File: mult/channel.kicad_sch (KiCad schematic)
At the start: 17 parts, among them J1 Eurorack_Mono_Jack, J2 Eurorack_Mono_Jack, J3 Eurorack_Mono_Jack_No_S, J4 Eurorack_Mono_Jack_No_S, U1 OPA1679

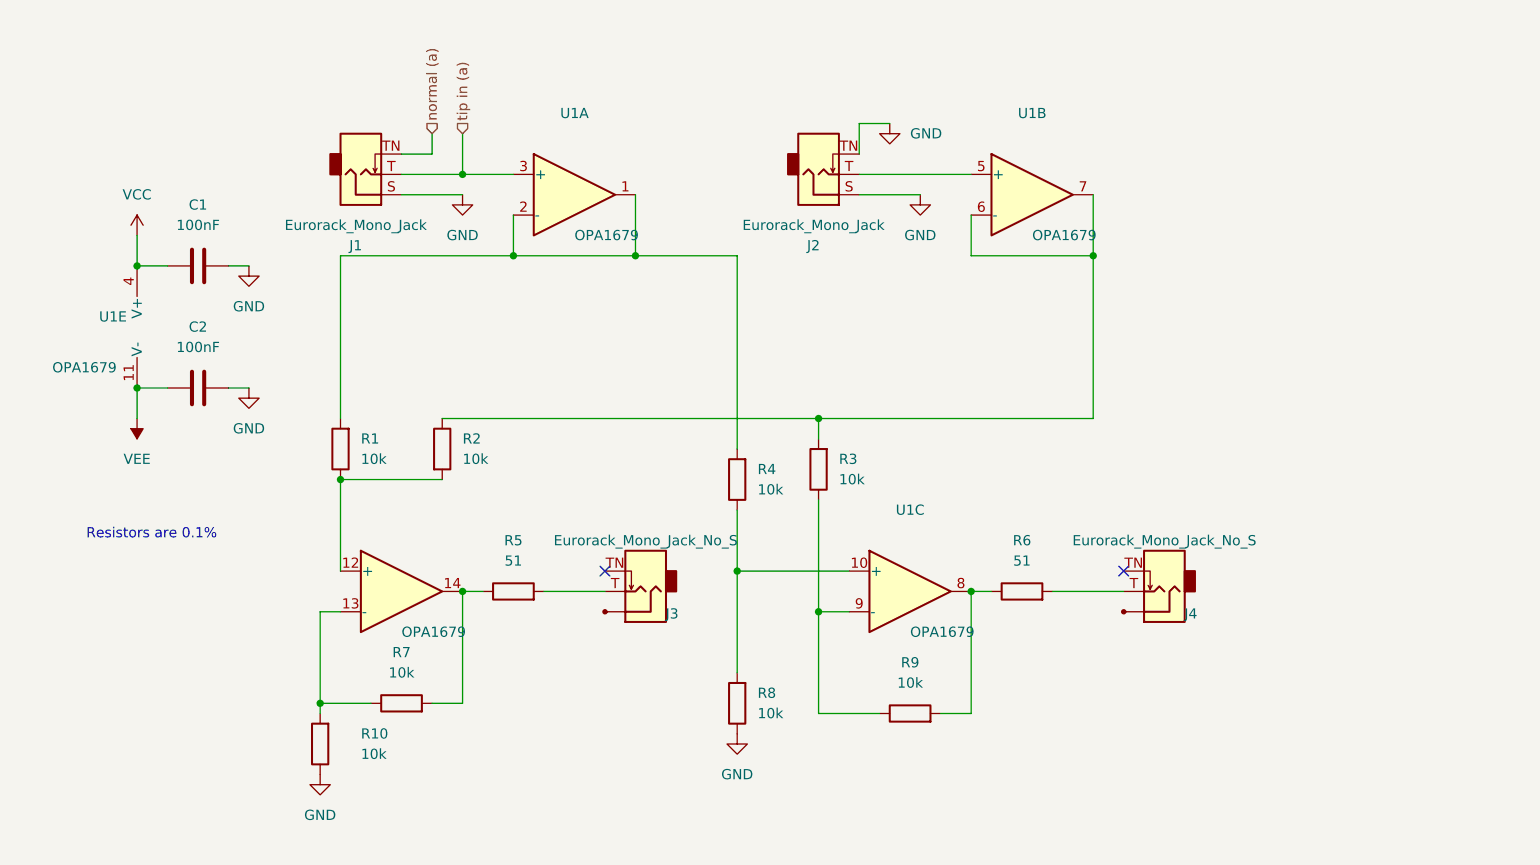
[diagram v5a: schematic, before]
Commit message: mult: Finish first layout pass, passes DRC errors
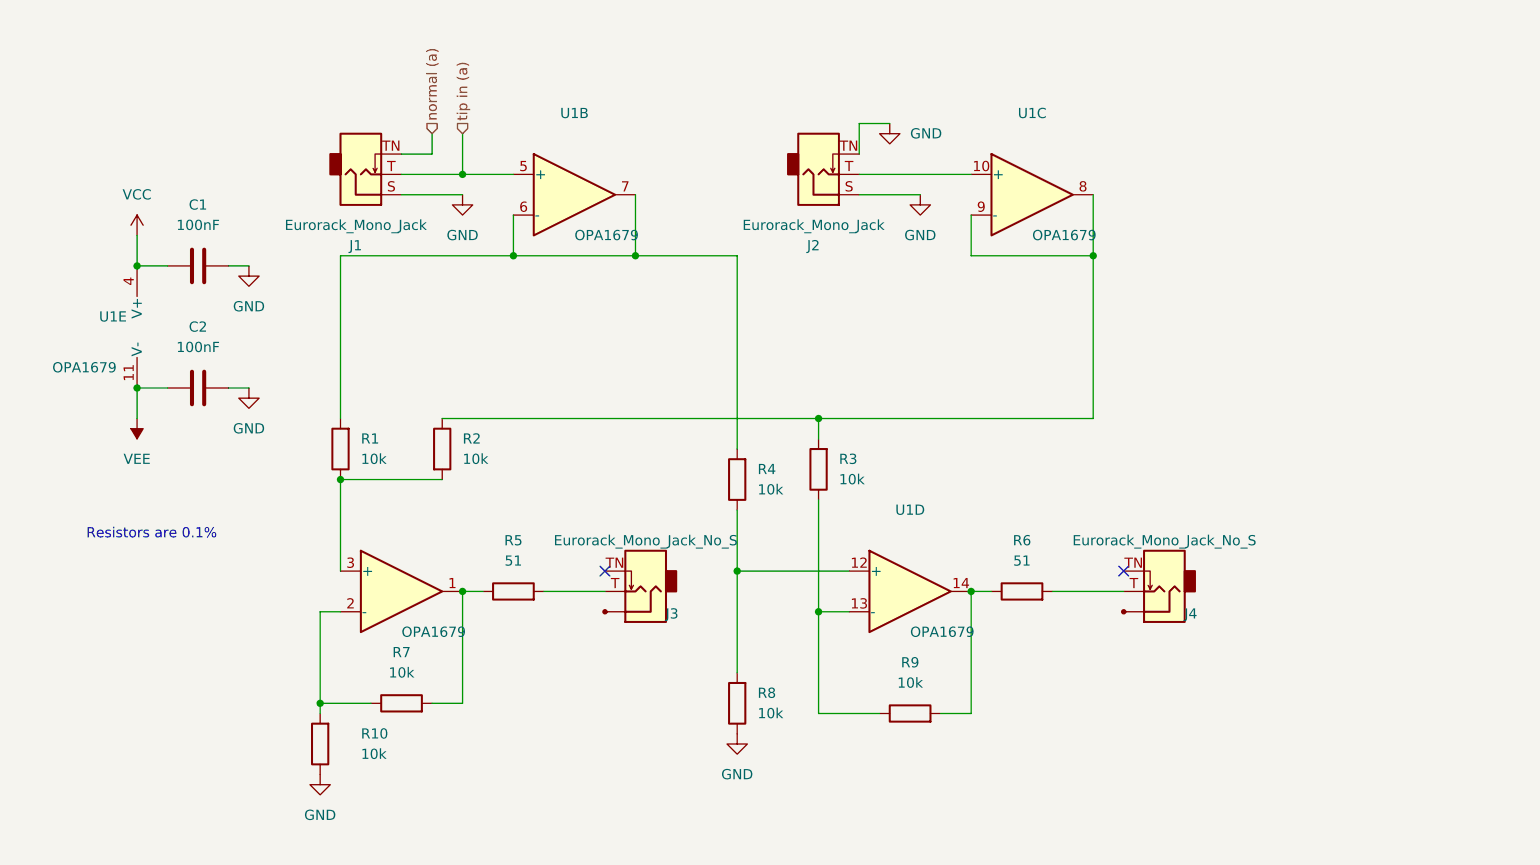
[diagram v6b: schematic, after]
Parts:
- U1: footprint Package_SO:TSSOP-14_4.4x5mm_P0.65mm -> Package_SO:SOIC-14_3.9x8.7mm_P1.27mm
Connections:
- net tip in (a): now also U1.5 (+); no longer U1.3 (+)
- net at J2.T (Tip): now also U1.10 (+); no longer U1.5 (+)
- net at R1.1, R2.2: now also U1.3 (+); no longer U1.12 (+)
- net at R10.2, R7.1: now also U1.2 (-); no longer U1.13 (-)
- net at R5.1, R7.2: now also U1.1; no longer U1.14
- net at R1.2, R4.2: now also U1.6 (-), U1.7; no longer U1.1, U1.2 (-)
- net at R2.1, R3.2: now also U1.8, U1.9 (-); no longer U1.6 (-), U1.7
- net at R4.1, R8.2: now also U1.12 (+); no longer U1.10 (+)
- net at R6.1, R9.2: now also U1.14; no longer U1.8
- net at R3.1, R9.1: now also U1.13 (-); no longer U1.9 (-)
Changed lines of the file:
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@@
     )
   )
-  (symbol (lib_id "Amplifier_Operational:OPA1679") (at 62.23 110.49 0) (unit 4)
+  (symbol (lib_id "Amplifier_Operational:OPA1679") (at 62.23 110.49 0) (unit 1)
     (in_bom yes) (on_board yes) (dnp no) (fields_autoplaced)
     (property "Reference" "U1" (at 62.23 100.33 0)
@@
       (effects (font (size 1.27 1.27)) (justify left))
     )
-    (property "Footprint" "Package_SO:TSSOP-14_4.4x5mm_P0.65mm" (at 60.96 107.95 0)
+    (property "Footprint" "Package_SO:SOIC-14_3.9x8.7mm_P1.27mm" (at 60.96 107.95 0)
       (effects (font (size 1.27 1.27)) hide)
     )
@@
       (project "mult"
         (path "/0e98ec4b-b4c7-447c-abd7-a761177a7f67/2249c80e-b931-4fee-ab04-d512ceb5f269"
-          (reference "U1") (unit 4)
-        )
-        (path "/0e98ec4b-b4c7-447c-abd7-a761177a7f67/b290c7a8-131c-4f39-ab4f-62063cf2647f"
-          (reference "U2") (unit 4)
-        )
-        (path "/0e98ec4b-b4c7-447c-abd7-a761177a7f67/b26d7339-1ce2-4103-8db8-9f6dbd3f09ef"
-          (reference "U3") (unit 4)
-        )
-        (path "/0e98ec4b-b4c7-447c-abd7-a761177a7f67/c8627544-d82d-426a-84eb-b4928bf7d17c"
-          (reference "U4") (unit 4)
-        )
-      )
-    )
-  )
-  (symbol (lib_id "Amplifier_Operational:OPA1679") (at 83.82 60.96 0) (unit 1)
+          (reference "U1") (unit 1)
+        )
+        (path "/0e98ec4b-b4c7-447c-abd7-a761177a7f67/b290c7a8-131c-4f39-ab4f-62063cf2647f"
+          (reference "U2") (unit 1)
+        )
+        (path "/0e98ec4b-b4c7-447c-abd7-a761177a7f67/b26d7339-1ce2-4103-8db8-9f6dbd3f09ef"
+          (reference "U3") (unit 1)
+        )
+        (path "/0e98ec4b-b4c7-447c-abd7-a761177a7f67/c8627544-d82d-426a-84eb-b4928bf7d17c"
+          (reference "U4") (unit 1)
+        )
+      )
+    )
+  )
+  (symbol (lib_id "Amplifier_Operational:OPA1679") (at 83.82 60.96 0) (unit 2)
     (in_bom yes) (on_board yes) (dnp no) (fields_autoplaced)
     (property "Reference" "U1" (at 83.82 50.8 0)
@@
       (effects (font (size 1.27 1.27)) (justify left))
     )
-    (property "Footprint" "Package_SO:TSSOP-14_4.4x5mm_P0.65mm" (at 82.55 58.42 0)
+    (property "Footprint" "Package_SO:SOIC-14_3.9x8.7mm_P1.27mm" (at 82.55 58.42 0)
       (effects (font (size 1.27 1.27)) hide)
     )
@@
       (project "mult"
         (path "/0e98ec4b-b4c7-447c-abd7-a761177a7f67/2249c80e-b931-4fee-ab04-d512ceb5f269"
-          (reference "U1") (unit 1)
-        )
-        (path "/0e98ec4b-b4c7-447c-abd7-a761177a7f67/b290c7a8-131c-4f39-ab4f-62063cf2647f"
-          (reference "U2") (unit 1)
-        )
-        (path "/0e98ec4b-b4c7-447c-abd7-a761177a7f67/b26d7339-1ce2-4103-8db8-9f6dbd3f09ef"
-          (reference "U3") (unit 1)
-        )
-        (path "/0e98ec4b-b4c7-447c-abd7-a761177a7f67/c8627544-d82d-426a-84eb-b4928bf7d17c"
-          (reference "U4") (unit 1)
+          (reference "U1") (unit 2)
+        )
+        (path "/0e98ec4b-b4c7-447c-abd7-a761177a7f67/b290c7a8-131c-4f39-ab4f-62063cf2647f"
+          (reference "U2") (unit 2)
+        )
+        (path "/0e98ec4b-b4c7-447c-abd7-a761177a7f67/b26d7339-1ce2-4103-8db8-9f6dbd3f09ef"
+          (reference "U3") (unit 2)
+        )
+        (path "/0e98ec4b-b4c7-447c-abd7-a761177a7f67/c8627544-d82d-426a-84eb-b4928bf7d17c"
+          (reference "U4") (unit 2)
         )
       )
@@
     )
   )
-  (symbol (lib_id "Amplifier_Operational:OPA1679") (at 125.73 110.49 0) (unit 3)
+  (symbol (lib_id "Amplifier_Operational:OPA1679") (at 125.73 110.49 0) (unit 4)
     (in_bom yes) (on_board yes) (dnp no)
     (property "Reference" "U1" (at 125.73 100.33 0)
@@
       (effects (font (size 1.27 1.27)) (justify left))
     )
-    (property "Footprint" "Package_SO:TSSOP-14_4.4x5mm_P0.65mm" (at 124.46 107.95 0)
+    (property "Footprint" "Package_SO:SOIC-14_3.9x8.7mm_P1.27mm" (at 124.46 107.95 0)
       (effects (font (size 1.27 1.27)) hide)
     )
@@
       (project "mult"
         (path "/0e98ec4b-b4c7-447c-abd7-a761177a7f67/2249c80e-b931-4fee-ab04-d512ceb5f269"
-          (reference "U1") (unit 3)
-        )
-        (path "/0e98ec4b-b4c7-447c-abd7-a761177a7f67/b290c7a8-131c-4f39-ab4f-62063cf2647f"
-          (reference "U2") (unit 3)
-        )
-        (path "/0e98ec4b-b4c7-447c-abd7-a761177a7f67/b26d7339-1ce2-4103-8db8-9f6dbd3f09ef"
-          (reference "U3") (unit 3)
-        )
-        (path "/0e98ec4b-b4c7-447c-abd7-a761177a7f67/c8627544-d82d-426a-84eb-b4928bf7d17c"
-          (reference "U4") (unit 3)
+          (reference "U1") (unit 4)
+        )
+        (path "/0e98ec4b-b4c7-447c-abd7-a761177a7f67/b290c7a8-131c-4f39-ab4f-62063cf2647f"
+          (reference "U2") (unit 4)
+        )
+        (path "/0e98ec4b-b4c7-447c-abd7-a761177a7f67/b26d7339-1ce2-4103-8db8-9f6dbd3f09ef"
+          (reference "U3") (unit 4)
+        )
+        (path "/0e98ec4b-b4c7-447c-abd7-a761177a7f67/c8627544-d82d-426a-84eb-b4928bf7d17c"
+          (reference "U4") (unit 4)
         )
       )
@@
     )
   )
-  (symbol (lib_id "Amplifier_Operational:OPA1679") (at 140.97 60.96 0) (unit 2)
+  (symbol (lib_id "Amplifier_Operational:OPA1679") (at 140.97 60.96 0) (unit 3)
     (in_bom yes) (on_board yes) (dnp no) (fields_autoplaced)
     (property "Reference" "U1" (at 140.97 50.8 0)
@@
       (effects (font (size 1.27 1.27)) (justify left))
     )
-    (property "Footprint" "Package_SO:TSSOP-14_4.4x5mm_P0.65mm" (at 139.7 58.42 0)
+    (property "Footprint" "Package_SO:SOIC-14_3.9x8.7mm_P1.27mm" (at 139.7 58.42 0)
       (effects (font (size 1.27 1.27)) hide)
     )
@@
       (project "mult"
         (path "/0e98ec4b-b4c7-447c-abd7-a761177a7f67/2249c80e-b931-4fee-ab04-d512ceb5f269"
-          (reference "U1") (unit 2)
-        )
-        (path "/0e98ec4b-b4c7-447c-abd7-a761177a7f67/b290c7a8-131c-4f39-ab4f-62063cf2647f"
-          (reference "U2") (unit 2)
-        )
-        (path "/0e98ec4b-b4c7-447c-abd7-a761177a7f67/b26d7339-1ce2-4103-8db8-9f6dbd3f09ef"
-          (reference "U3") (unit 2)
-        )
-        (path "/0e98ec4b-b4c7-447c-abd7-a761177a7f67/c8627544-d82d-426a-84eb-b4928bf7d17c"
-          (reference "U4") (unit 2)
+          (reference "U1") (unit 3)
+        )
+        (path "/0e98ec4b-b4c7-447c-abd7-a761177a7f67/b290c7a8-131c-4f39-ab4f-62063cf2647f"
+          (reference "U2") (unit 3)
+        )
+        (path "/0e98ec4b-b4c7-447c-abd7-a761177a7f67/b26d7339-1ce2-4103-8db8-9f6dbd3f09ef"
+          (reference "U3") (unit 3)
+        )
+        (path "/0e98ec4b-b4c7-447c-abd7-a761177a7f67/c8627544-d82d-426a-84eb-b4928bf7d17c"
+          (reference "U4") (unit 3)
         )
       )
@@
       (effects (font (size 1.27 1.27)) (justify left))
     )
-    (property "Footprint" "Package_SO:TSSOP-14_4.4x5mm_P0.65mm" (at 27.94 74.93 0)
-      (effects (font (size 1.27 1.27)) hide)
-    )
+    (property "Footprint" "Package_SO:SOIC-14_3.9x8.7mm_P1.27mm" (at 27.94 74.93 0)
+      (effects (font (size 1.27 1.27)) hide)
+    )

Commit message: mult: Reassign reference designators
This follows visual placement (left to right, top to bottom), except for
bulk capacitors which are enumerated left to right after bypass caps.
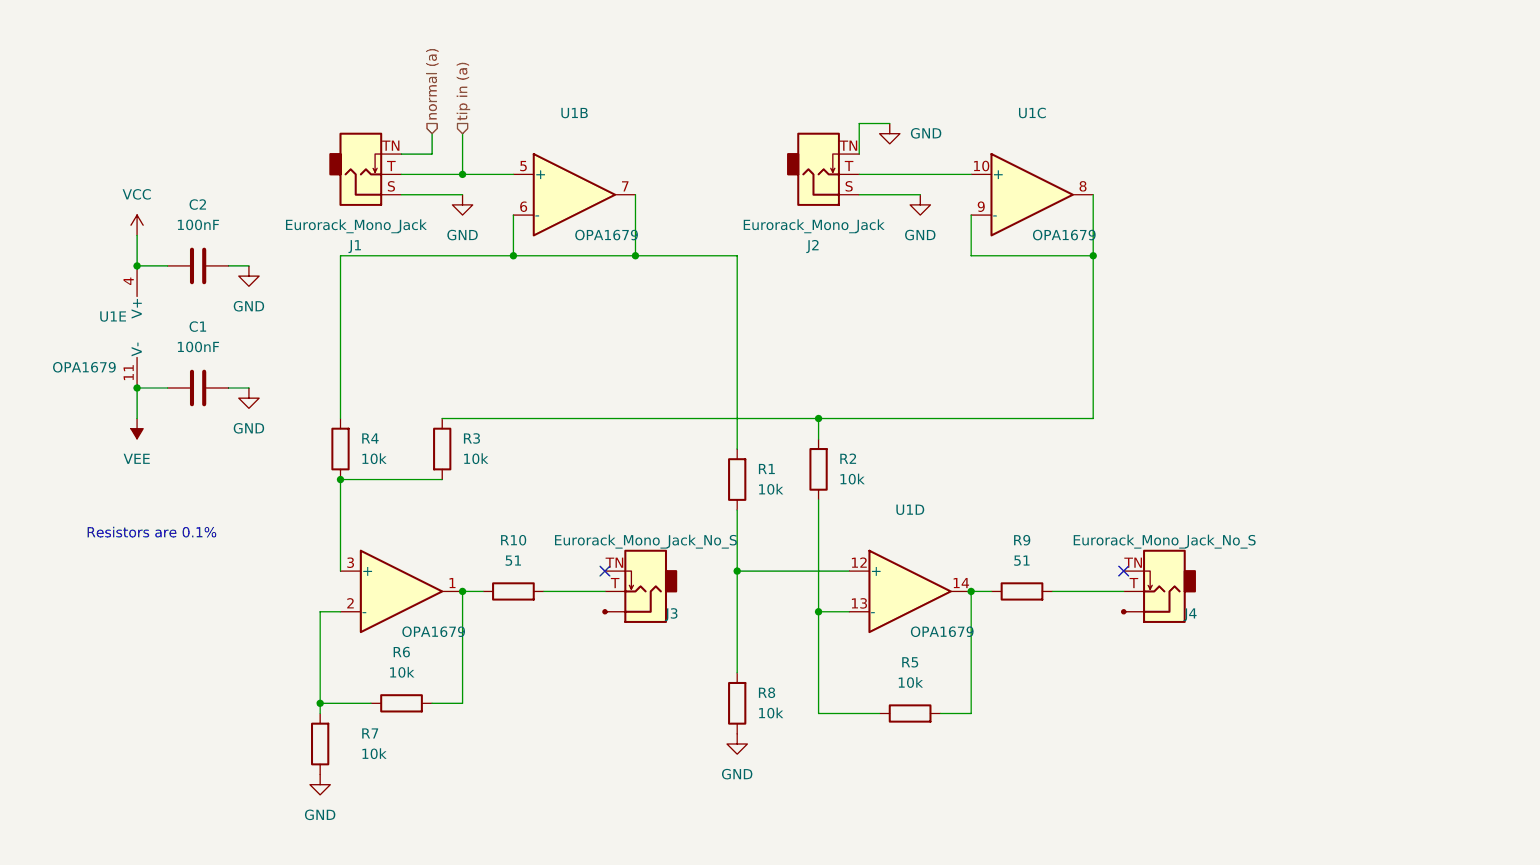
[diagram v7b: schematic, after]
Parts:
- renumbered C2 to C1, C1 to C2, R4 to R1, R5 to R10, R3 to R2, R2 to R3, R1 to R4, R9 to R5, R7 to R6, R10 to R7, R6 to R9
